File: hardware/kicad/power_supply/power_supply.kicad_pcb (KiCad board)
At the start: 2 copper layers, 35 parts, among them J1 PINHD_1x4_Female, J2 USB_C_Receptacle_PowerOnly_6P, J3 USB_C_Receptacle_PowerOnly_6P, Q1 AO3401A, U1 MT3608, U2 TP4056-42-ESOP8

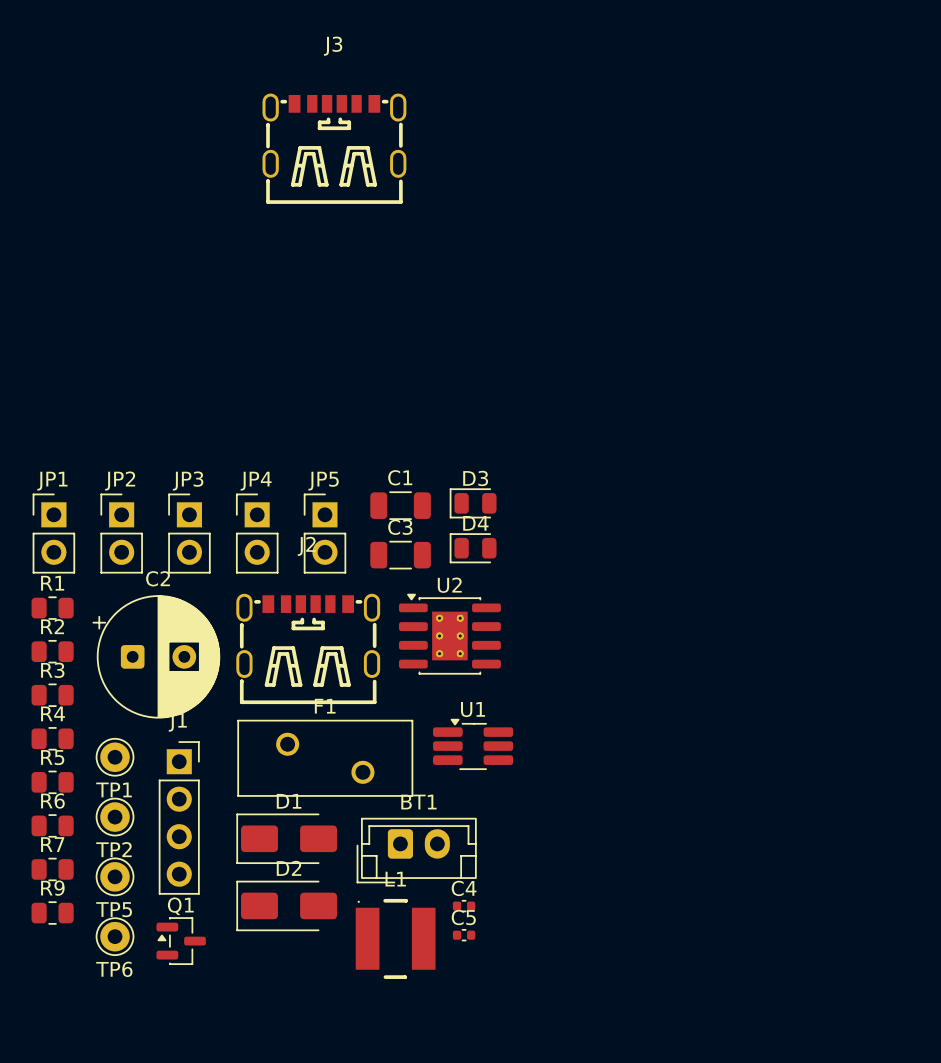
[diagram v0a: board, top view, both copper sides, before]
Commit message: First draft completed for the power supply kicad project
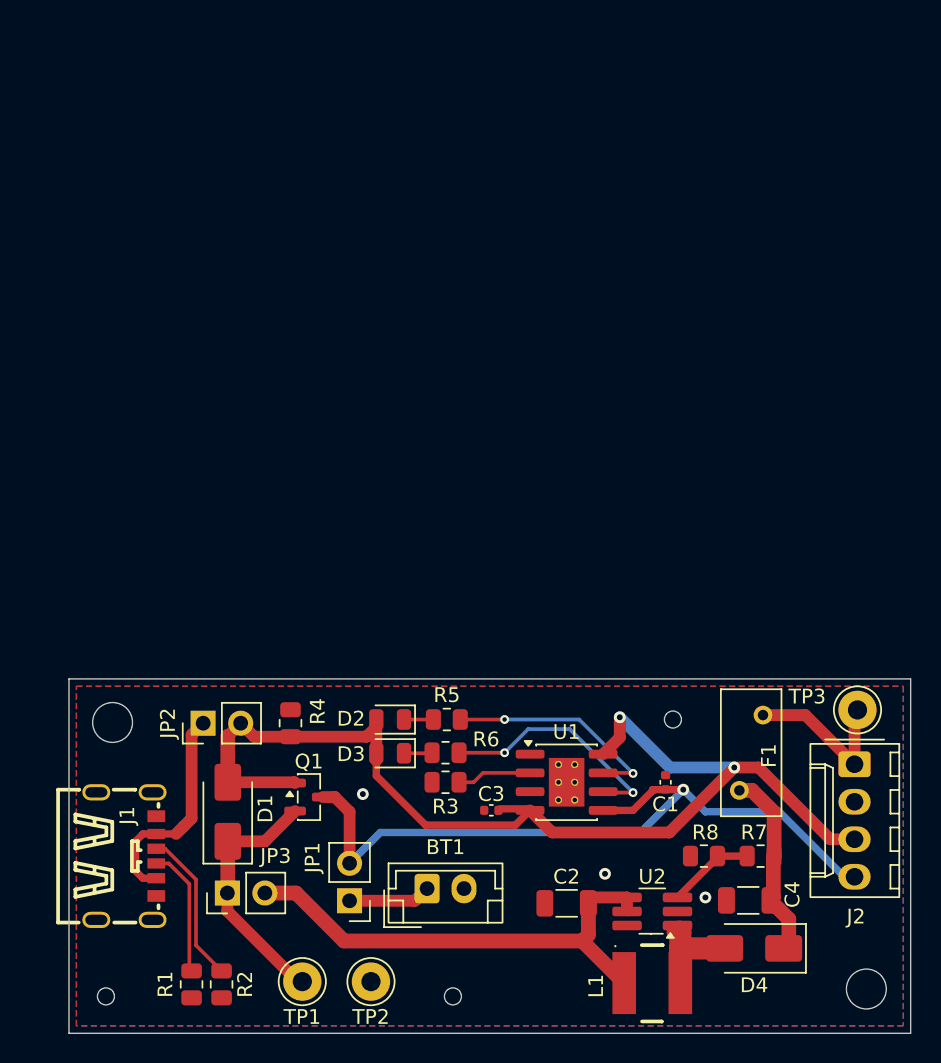
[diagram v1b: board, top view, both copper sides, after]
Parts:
- removed C5: 10uF, Capacitor_SMD:C_0402_1005Metric
- removed J3: USB_C_Receptacle_PowerOnly_6P, JLCPCB:TYPE-C-SMD_TYPE-C-6P
- removed JP4, JP5: Jumper_2_Small_Bridged, Connector_PinHeader_2.54mm:PinHeader_1x02_P2.54mm_Vertical
- removed R9: 1k, Resistor_SMD:R_0805_2012Metric
- removed TP5, TP6: TestPoint, Connector_Pin:Pin_D1.0mm_L10.0mm
- added M1: MountingHole_2.7mm, PowerSupply:MountingHole_2.7mm, F.Cu at (119.3, 85.2)
- added M2: MountingHole_2.7mm, PowerSupply:MountingHole_2.7mm, F.Cu at (170.3, 103.2)
- added M3: MountingHole_2.2mm_M2, PowerSupply:MountingHole_2.2mm_M2, F.Cu at (118.8, 103.7)
- added M4: MountingHole_2.2mm_M2, PowerSupply:MountingHole_2.2mm_M2, F.Cu at (142.3, 103.7)
- added M5: MountingHole_2.2mm_M2, PowerSupply:MountingHole_2.2mm_M2, F.Cu at (157.2, 85.0)
- added R8: 15k, PowerSupply:R_0805_2012Metric, F.Cu at (159.3, 94.2)
- added TP3: out, PowerSupply:Pin_D1.3mm_L11.0mm, F.Cu at (169.7, 84.3)
- BT1: footprint Connector_JST:JST_EH_B2B-EH-A_1x02_P2.50mm_Vertical -> PowerSupply:JST_EH_B2B-EH-A_1x02_P2.50mm_Vertical
- C1, C3: value 22uF -> 10uF; footprint Capacitor_SMD:C_1206_3216Metric -> PowerSupply:C_0402_1005Metric
- C2: value 470uF -> 22uF; footprint Capacitor_THT:CP_Radial_D8.0mm_P3.50mm -> PowerSupply:C_1206_3216Metric
- C4: value 10uF -> 22uF; footprint Capacitor_SMD:C_0402_1005Metric -> PowerSupply:C_1206_3216Metric
- D1: footprint Diode_SMD:D_SMA -> PowerSupply:D_SMA
- D2: value SS34 -> RED; footprint Diode_SMD:D_SMA -> PowerSupply:LED_0805_2012Metric
- D3: value RED -> GREEN; footprint LED_SMD:LED_0805_2012Metric -> PowerSupply:LED_0805_2012Metric
- D4: value GREEN -> SS34; footprint LED_SMD:LED_0805_2012Metric -> PowerSupply:D_SMA
- F1: footprint Fuse:Fuse_BelFuse_0ZRE0075FF_L11.5mm_W4.8mm -> PowerSupply:Fuse_BelFuse_0ZRE0005FF_L8.3mm_W3.8mm
- J1: value PINHD_1x4_Female -> USB_C_Receptacle_PowerOnly_6P; footprint Connector_PinSocket_2.54mm:PinSocket_1x04_P2.54mm_Vertical -> PowerSupply:TYPE-C-SMD_TYPE-C-6P
- J2: value USB_C_Receptacle_PowerOnly_6P -> PINHD_1x4_Female; footprint JLCPCB:TYPE-C-SMD_TYPE-C-6P -> PowerSupply:Molex_KK-254_AE-6410-04A_1x04_P2.54mm_Vertical
- JP1: value Jumper_2_Bridged -> Bat; footprint Connector_PinHeader_2.54mm:PinHeader_1x02_P2.54mm_Vertical -> PowerSupply:PinHeader_1x02_P2.54mm_Vertical
- JP2: value Jumper_2_Small_Bridged -> usb; footprint Connector_PinHeader_2.54mm:PinHeader_1x02_P2.54mm_Vertical -> PowerSupply:PinHeader_1x02_P2.54mm_Vertical
- JP3: value Jumper_2_Small_Bridged -> power; footprint Connector_PinHeader_2.54mm:PinHeader_1x02_P2.54mm_Vertical -> PowerSupply:PinHeader_1x02_P2.54mm_Vertical
- L1: footprint JLCPCB:IND-SMD_2P-L5.0-W5.0 -> PowerSupply:IND-SMD_2P-L5.0-W5.0
- Q1: footprint Package_TO_SOT_SMD:SOT-23 -> PowerSupply:SOT-23
- R1: value 110k -> 5.1k; footprint Resistor_SMD:R_0805_2012Metric -> PowerSupply:R_0805_2012Metric
- R2: value 15k -> 5.1k; footprint Resistor_SMD:R_0805_2012Metric -> PowerSupply:R_0805_2012Metric
- R3: value 100k -> 2.4k; footprint Resistor_SMD:R_0805_2012Metric -> PowerSupply:R_0805_2012Metric
- R4: value 5.1k -> 100k; footprint Resistor_SMD:R_0805_2012Metric -> PowerSupply:R_0805_2012Metric
- R5: value 5.1k -> 1k; footprint Resistor_SMD:R_0805_2012Metric -> PowerSupply:R_0805_2012Metric
- R6: value 2.4k -> 1k; footprint Resistor_SMD:R_0805_2012Metric -> PowerSupply:R_0805_2012Metric
- R7: value 1k -> 110k; footprint Resistor_SMD:R_0805_2012Metric -> PowerSupply:R_0805_2012Metric
- TP1: footprint Connector_Pin:Pin_D1.0mm_L10.0mm -> PowerSupply:Pin_D1.3mm_L11.0mm
- TP2: value TestPoint -> gnd; footprint Connector_Pin:Pin_D1.0mm_L10.0mm -> PowerSupply:Pin_D1.3mm_L11.0mm
- U1: value MT3608 -> TP4056-42-ESOP8; footprint Package_TO_SOT_SMD:TSOT-23-6_HandSoldering -> PowerSupply:SOIC-8-1EP_3.9x4.9mm_P1.27mm_EP2.41x3.3mm_ThermalVias
- U2: value TP4056-42-ESOP8 -> MT3608; footprint Package_SO:SOIC-8-1EP_3.9x4.9mm_P1.27mm_EP2.41x3.3mm_ThermalVias -> PowerSupply:TSOT-23-6_HandSoldering
- moved R7 48.0 mm to (163.1, 94.2), turned to 180 degrees
- moved J2 38.0 mm to (169.5, 88.0), turned to -90 degrees
- moved C2 33.8 mm to (150.0, 97.4), turned to 180 degrees
- moved D4 33.0 mm to (162.7, 100.5), turned to 180 degrees
- moved JP1 32.9 mm to (135.3, 97.3), turned to 180 degrees
- moved F1 30.8 mm to (161.7, 89.8), turned to 90 degrees
- moved R3 27.3 mm to (141.8, 89.2), turned to 180 degrees
- moved R1 27.2 mm to (124.6, 102.9), turned to -90 degrees
- moved R6 27.1 mm to (141.8, 87.2)
- moved R5 27.0 mm to (141.9, 85.0)
- moved C1 25.9 mm to (156.7, 89.2), turned to 90 degrees
- moved JP3 25.7 mm to (127.0, 96.7), turned to 90 degrees
- moved R2 25.3 mm to (126.6, 102.9), turned to -90 degrees
- moved U2 23.2 mm to (155.8, 98.0), turned to 180 degrees
- moved TP2 20.6 mm to (136.8, 102.7)
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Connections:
- C1 pad 1: Net-(D1-K) -> V_{bat}
- C2 pad 1: Net-(D1-K) -> Net-(JP3-B)
- C3 pad 1: Net-(JP1-B) -> V_{in}
- C4 pad 1: Net-(JP5-B) -> Net-(D4-K)
- D1 pad 2: Net-(D1-A) -> V_{in}
- D2 pad 2: Vusb -> V_{in}
- D3 pad 2: Net-(D3-A) -> V_{in}
- D4 pad 2: Net-(D3-A) -> Net-(D4-A)
- F1 pad 1: Net-(D1-K) -> Net-(D4-K)
- F1 pad 2: Net-(J1-Vout) -> Net-(J2-Vout)
- JP1 pad 1: Net-(D2-K) -> Net-(BT1-+)
- JP1 pad 2: Net-(JP1-B) -> V_{bat}
- JP2 pad 2: Vusb -> V_{in}
- JP3 pad 1: Net-(BT1-+) -> Net-(D1-K)
- JP3 pad 2: Vbat -> Net-(JP3-B)
- L1 pad 1: Net-(JP1-B) -> Net-(JP3-B)
- L1 pad 2: Net-(D1-A) -> Net-(D4-A)
- Q1 pad 1: Vusb -> V_{in}
- Q1 pad 2: Net-(D2-K) -> Net-(D1-K)
- Q1 pad 3: Vbat -> V_{bat}
- R1 pad 1: Net-(D1-K) -> Net-(J1-CC2)
- R1 pad 2: Net-(U1-FB) -> GND
- R2 pad 1: Net-(U1-FB) -> Net-(J1-CC1)
- R3 pad 1: Vusb -> Net-(U1-PROG)
- R4 pad 1: Net-(J3-CC2) -> V_{in}
- R5 pad 1: Net-(J3-CC1) -> Net-(D2-K)
- R5 pad 2: GND -> Net-(U1-~{CHRG})
- R6 pad 1: Net-(U2-PROG) -> Net-(D3-K)
- R6 pad 2: GND -> Net-(U1-~{STDBY})
- R7 pad 1: Net-(D3-K) -> Net-(D4-K)
- R7 pad 2: Net-(U2-~{CHRG}) -> Net-(U2-FB)
- TP1 pad 1: unconnected-(TP1-Pad1) -> Net-(D1-K)
- TP2 pad 1: Net-(J1-Vout) -> GND
- U1 pad 1: Net-(D1-A) -> GND
- U1 pad 2: GND -> Net-(U1-PROG)
- U1 pad 3: Net-(U1-FB) -> GND
- U1 pad 4: Net-(JP1-B) -> V_{in}
- U1 pad 5: Net-(JP1-B) -> V_{bat}
- U1 pad 6: unconnected-(U1-NC-Pad6) -> Net-(U1-~{STDBY})
- U2 pad 1: GND -> Net-(D4-A)
- U2 pad 2: Net-(U2-PROG) -> GND
- U2 pad 3: GND -> Net-(U2-FB)
- U2 pad 4: Net-(D3-A) -> Net-(JP3-B)
- U2 pad 5: Net-(JP5-B) -> Net-(JP3-B)
- U2 pad 6: Net-(U2-~{STDBY}) -> unconnected-(U2-NC-Pad6)
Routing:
- net V_{in}: track 0.00 -> 76.5 mm, vias 0 -> 2
- net V_{bat}: track 0.00 -> 50.8 mm, vias 0 -> 1
- net Net-(JP3-B): track 0.00 -> 33.2 mm
- net Net-(D1-K): track 0.00 -> 17.4 mm
- net Net-(U1-~{STDBY}): track 0.00 -> 16.3 mm, vias 0 -> 2
- net Net-(U1-~{CHRG}): track 0.00 -> 15.3 mm, vias 0 -> 2
- net Net-(JP2-A): track 0.00 -> 15.0 mm
- net Net-(D4-K): track 0.00 -> 12.8 mm
- net Net-(J2-Vout): track 0.00 -> 11.8 mm
- net Net-(J1-CC1): track 0.00 -> 10.5 mm
- net Net-(J1-CC2): track 0.00 -> 8.76 mm
- net Net-(D4-A): track 0.00 -> 7.01 mm
- net Net-(U2-FB): track 0.00 -> 6.11 mm
- net Net-(BT1-+): track 0.00 -> 5.59 mm
- net Net-(U1-PROG): track 0.00 -> 5.08 mm
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- added copper zone on B.Cu, net GND
- added copper zone on F.Cu, net GND
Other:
- board outline added: 57 x 24 mm

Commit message: Final version for power supply circuit
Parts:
- added M6: MountingHole_2.7mm, PowerSupply:MountingHole_2.7mm, F.Cu at (148.1, 103.2)
- moved BT1 0.79 mm to (140.8, 95.7)
- moved C2 0.78 mm to (150.6, 98.0), turned to 90 degrees
- moved J2 0.55 mm to (169.5, 88.6)
- moved TP3 0.55 mm to (169.7, 84.9)
- moved D4 0.40 mm to (162.3, 100.5)
- moved L1 0.35 mm to (155.8, 102.5)
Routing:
- net GND: track 0.35 -> 5.25 mm, vias 3 -> 9
- net Net-(D4-A): track 7.01 -> 9.33 mm
- net Net-(BT1-+): track 5.59 -> 6.45 mm
